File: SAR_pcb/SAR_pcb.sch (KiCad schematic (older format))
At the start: 32 parts, among them J1 Conn_Coaxial_Power, J10 Conn_Coaxial, J11 Conn_Coaxial, J13 Conn_01x10_Male, J2 Conn_Coaxial_Power, J3 Conn_Coaxial_Power, J4 Conn_Coaxial_Power, J5 Conn_Coaxial_Power, J6 Conn_01x02_Male, J7 Conn_01x02_Male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

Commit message: Added EP pin to SAR symbol
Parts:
- U2: symbol SAR_ADC:10B_SAR -> SAR_pcb-rescue:10B_SAR-SAR_ADC
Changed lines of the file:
@@
 	6250 5800 6250 5900
 $Comp
-L SAR_ADC:10B_SAR U2
+L SAR_pcb-rescue:10B_SAR-SAR_ADC U2
 U 1 1 5F7A3A6A
 P 5250 4450
@@
 	1    0    0    -1
 $EndComp
+$Comp
+L power:GND #PWR?
+U 1 1 5F7D0630
+P 6650 5650
+F 0 "#PWR?" H 6650 5400 50  0001 C CNN
+F 1 "GND" H 6655 5477 50  0000 C CNN
+F 2 "" H 6650 5650 50  0001 C CNN
+F 3 "" H 6650 5650 50  0001 C CNN
+	1    6650 5650
+	0    -1   -1   0
+$EndComp
 $EndSCHEMATC

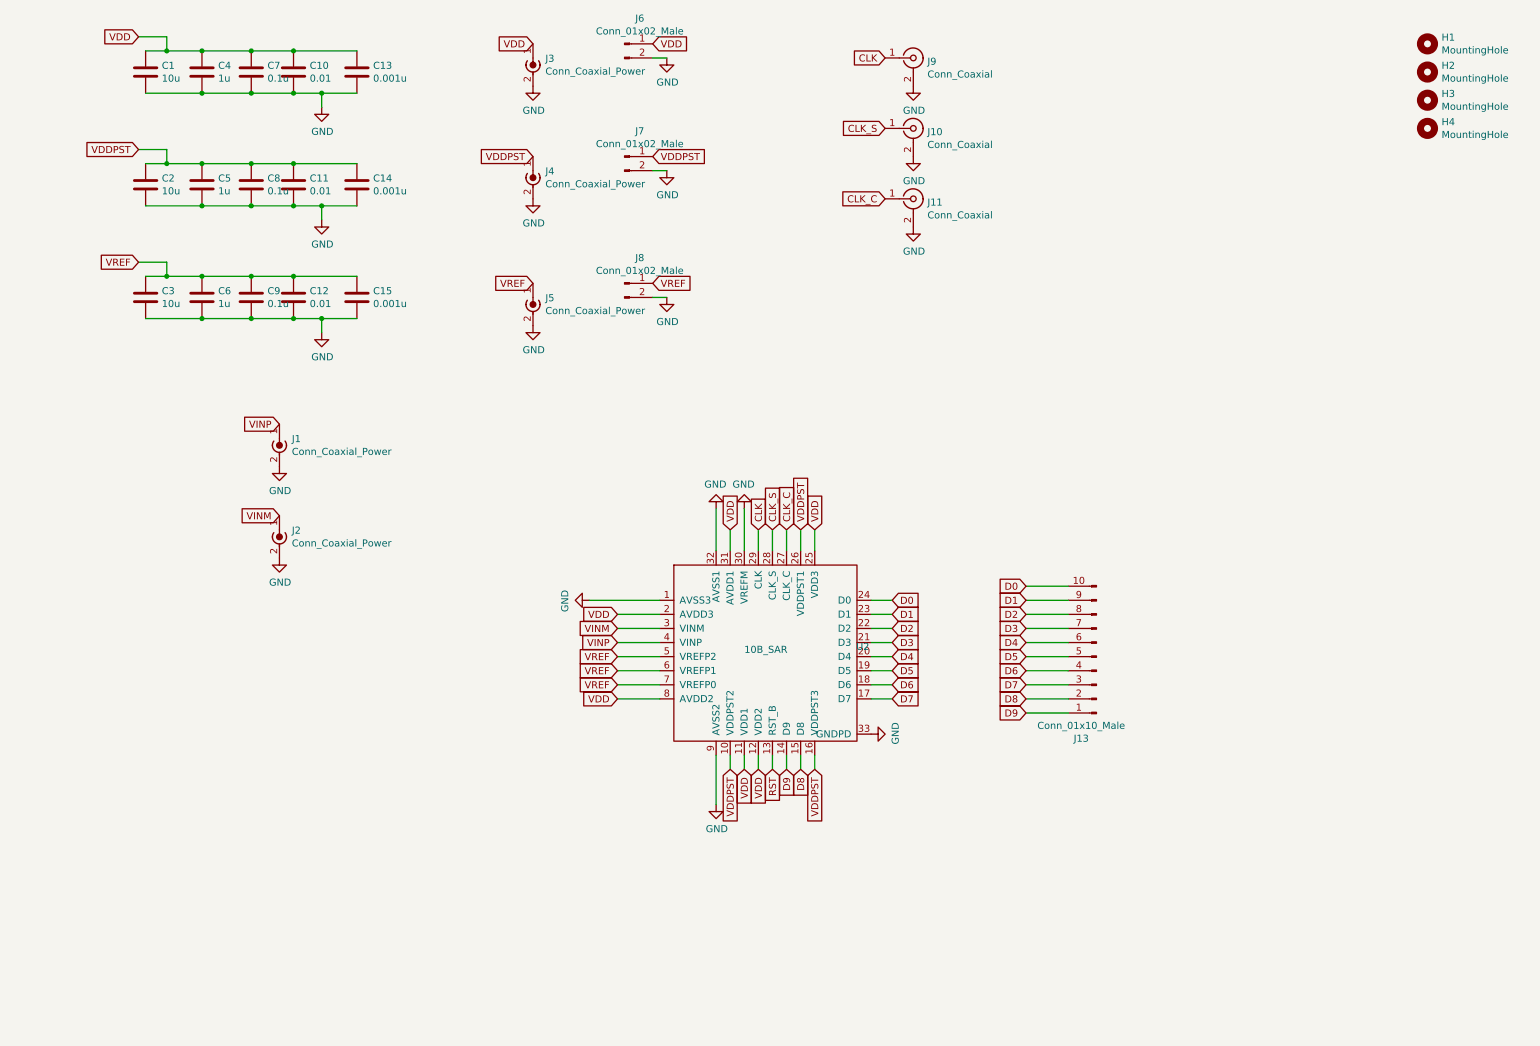
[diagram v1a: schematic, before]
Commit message: Fixed Vin notation for differential net, switched to using 2-pin digital outputs for high speed adapter
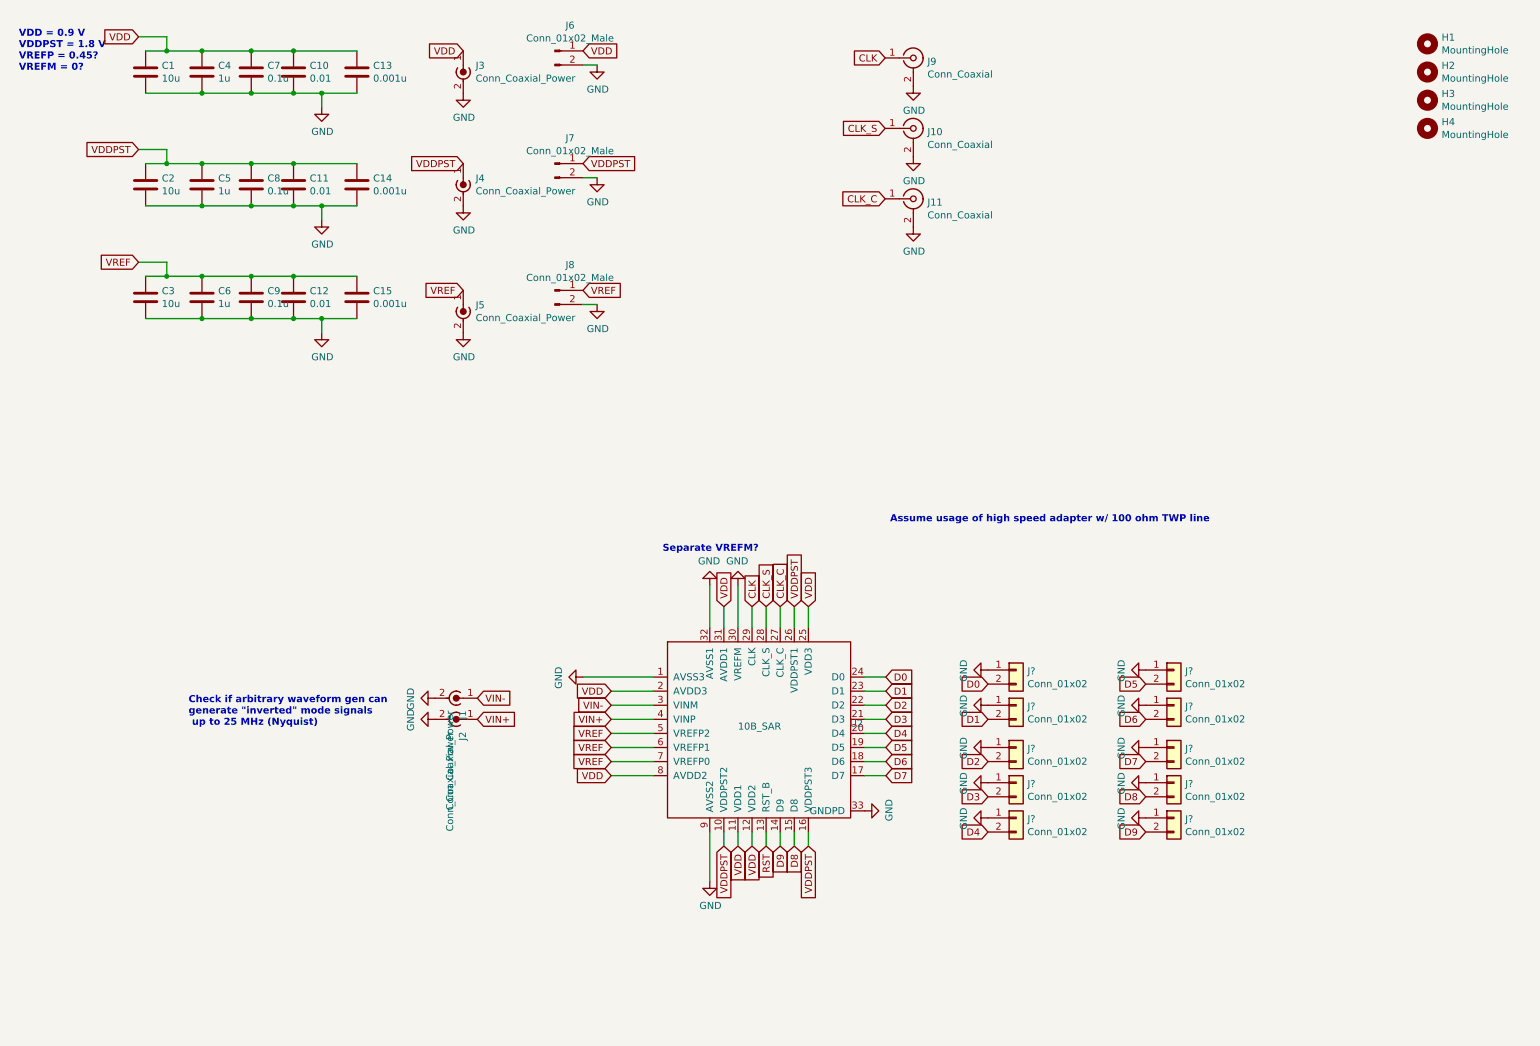
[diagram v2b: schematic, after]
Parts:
- removed J13: Conn_01x10_Male, Connector_Molex:Molex_KK-254_AE-6410-10A_1x10_P2.54mm_Vertical, symbol Connector:Conn_01x10_Male
- added J? (x10): Conn_01x02, Connector_PinHeader_2.54mm:PinHeader_1x02_P2.54mm_Vertical, symbol Connector_Generic:Conn_01x02
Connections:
- net D0: now also J?.2 (Pin_2)
- net D1: now also J?.2 (Pin_2)
- net D2: now also J?.2 (Pin_2)
- net D3: now also J?.2 (Pin_2)
- net D4: now also J?.2 (Pin_2)
- net D5: now also J?.2 (Pin_2)
- net D6: now also J?.2 (Pin_2)
- net D7: now also J?.2 (Pin_2)
- net D8: now also J?.2 (Pin_2)
- net D9: now also J?.2 (Pin_2)
- net GND: now also J?.1 (Pin_1), J?.1 (Pin_1), J?.1 (Pin_1), J?.1 (Pin_1), J?.1 (Pin_1), J?.1 (Pin_1), J?.1 (Pin_1), J?.1 (Pin_1), J?.1 (Pin_1), J?.1 (Pin_1)
- net VINM renamed VIN+
- net VIN+: now also U2.4 (VINP); no longer U2.3 (VINM)
- net VINP renamed VIN-
- net VIN-: now also U2.3 (VINM); no longer U2.4 (VINP)
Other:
- note added: "Assume usage of high speed adapter w/ 100 ohm TWP line"
- note added: "Check if arbitrary waveform gen can \ngenerate "inverted" mode signals\n up to 25 MHz (Nyquist)"
- note added: "Separate VREFM?"
- note added: "VDD = 0.9 V\nVDDPST = 1.8 V\nVREFP = 0.45?\nVREFM = 0?"
- moved on the sheet: J1, J2, J3, J4, J5, J6, J7, J8, U2

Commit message: Added stackup PDF, corrected Board Setup in pcbnew
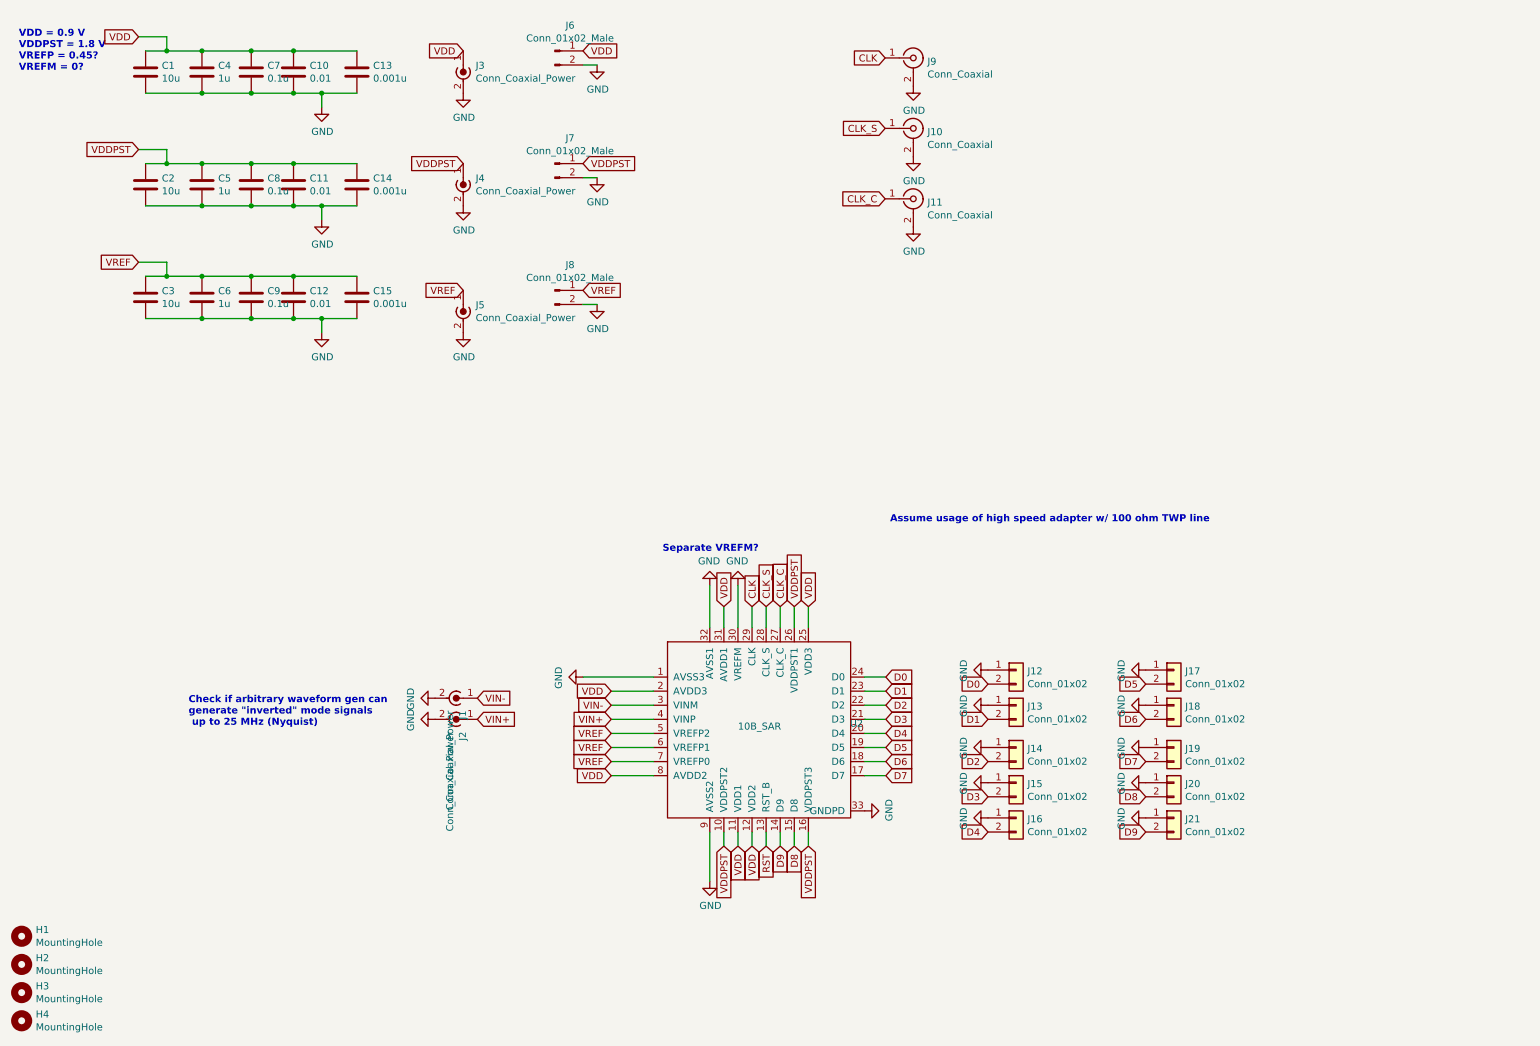
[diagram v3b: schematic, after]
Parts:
- J10, J11, J9: footprint Connector_Coaxial:SMA_Amphenol_132291_Vertical -> Connector_Coaxial:SMA_Amphenol_132289_EdgeMount
- gave numbers to parts that had none: 10
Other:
- moved on the sheet: H1, H2, H3, H4
